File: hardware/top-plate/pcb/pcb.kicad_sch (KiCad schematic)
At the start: 43 parts, among them SW1 MT-0-102-A101-M200-RS+PJ

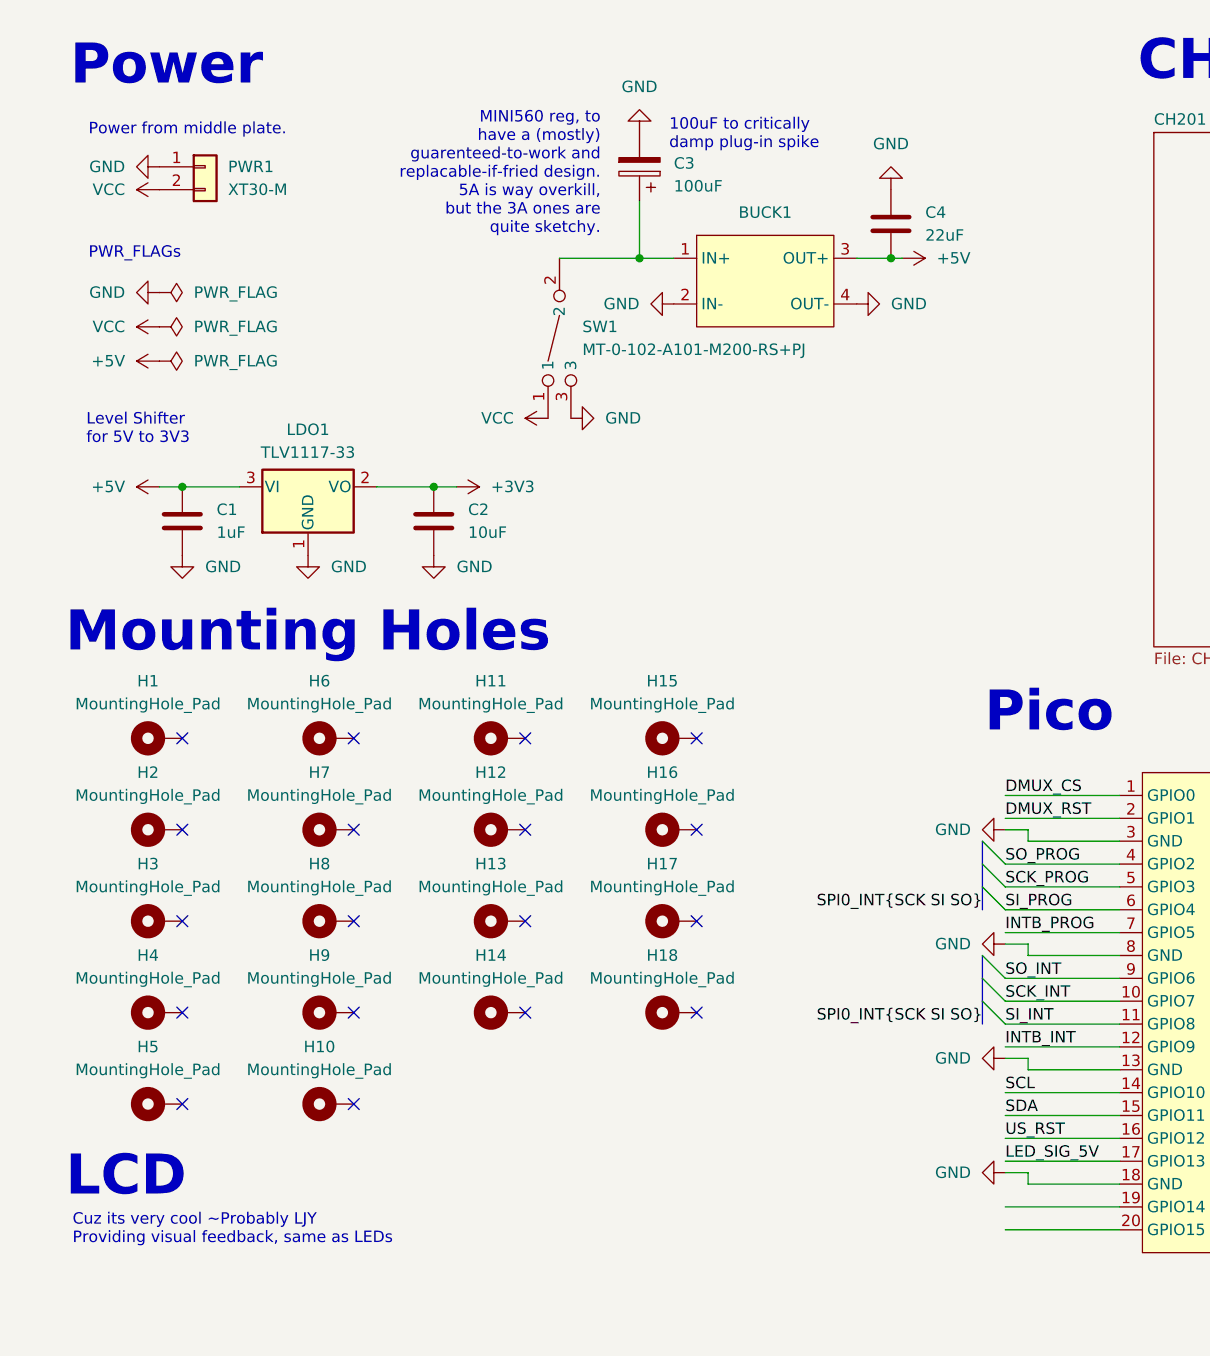
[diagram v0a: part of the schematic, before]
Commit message: changed some reference designators, and cleaned up schematics
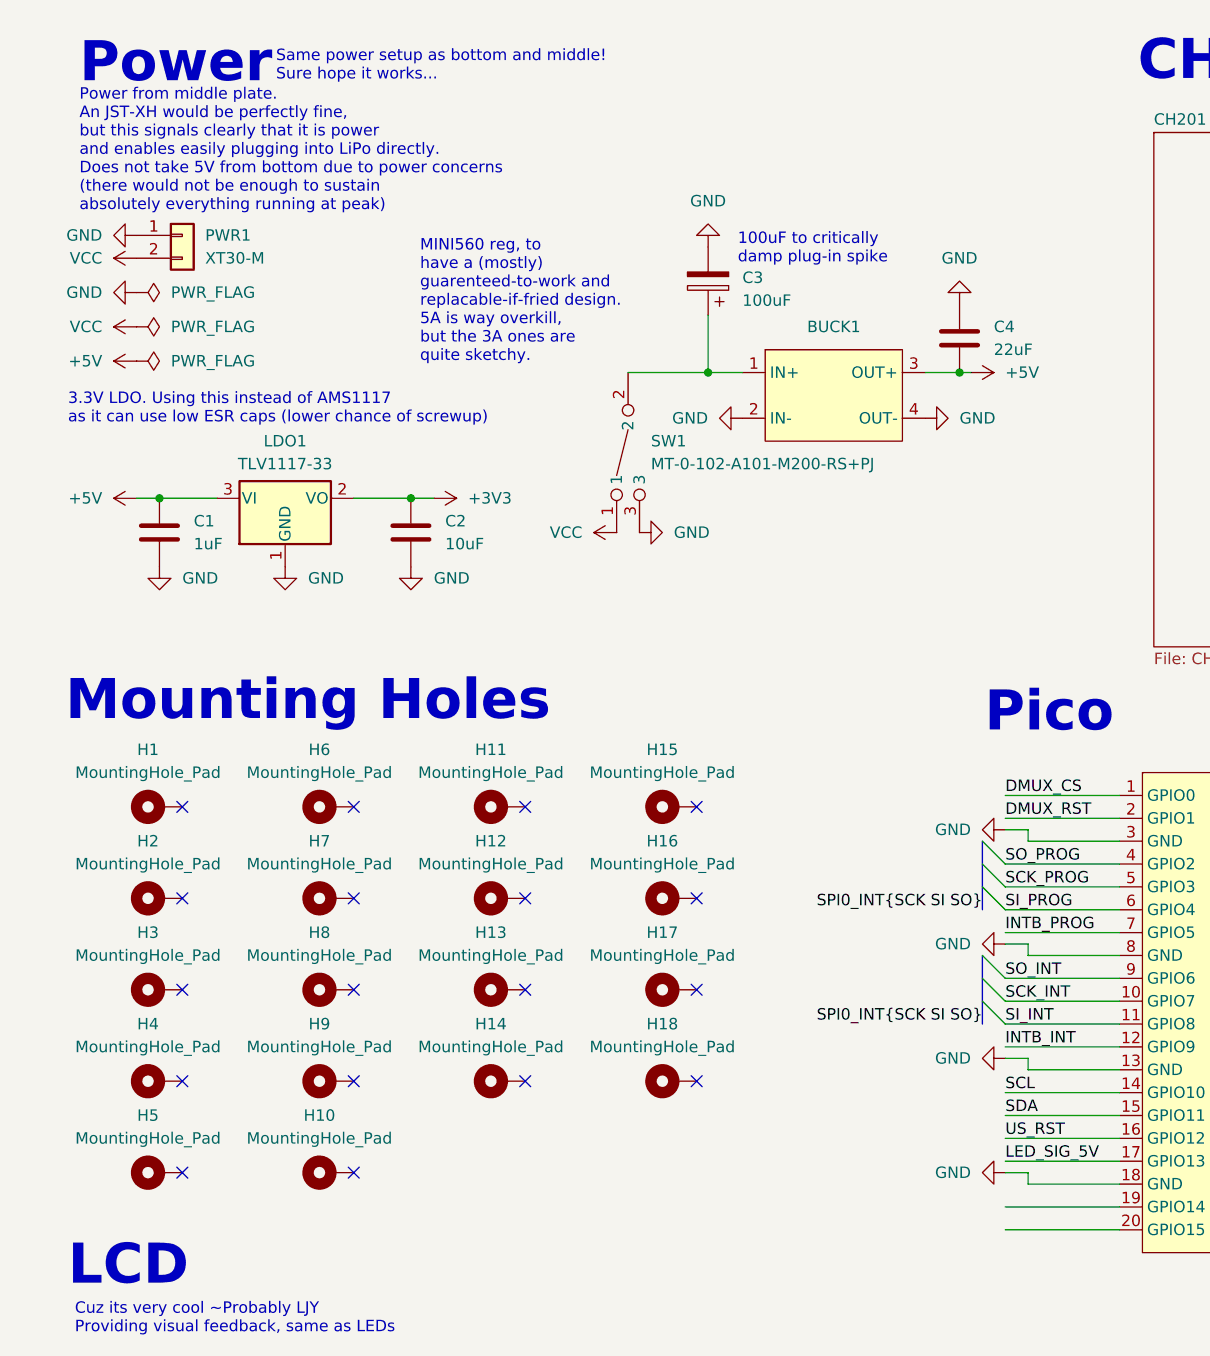
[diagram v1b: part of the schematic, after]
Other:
- note added: "3.3V LDO. Using this instead of AMS1117 as it can use low ESR caps (lower chance of screwup)"
- note added: "Power from middle plate. An JST-XH would be perfectly fine, but this signals clearly that it is power and enables easily plugging into LiPo directly. Does not take 5V from bottom due to power concerns (there would not be enough to sustain absolutely everything running at peak)"
- note added: "Same power setup as bottom and middle! Sure hope it works..."
- note removed: "Level Shifter for 5V to 3V3"
- note removed: "PWR_FLAGs"
- note removed: "Power from middle plate."
- moved on the sheet: BUCK1, C1, C2, C3, C4, H1, H10, H11, H12, H13, H14, H15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

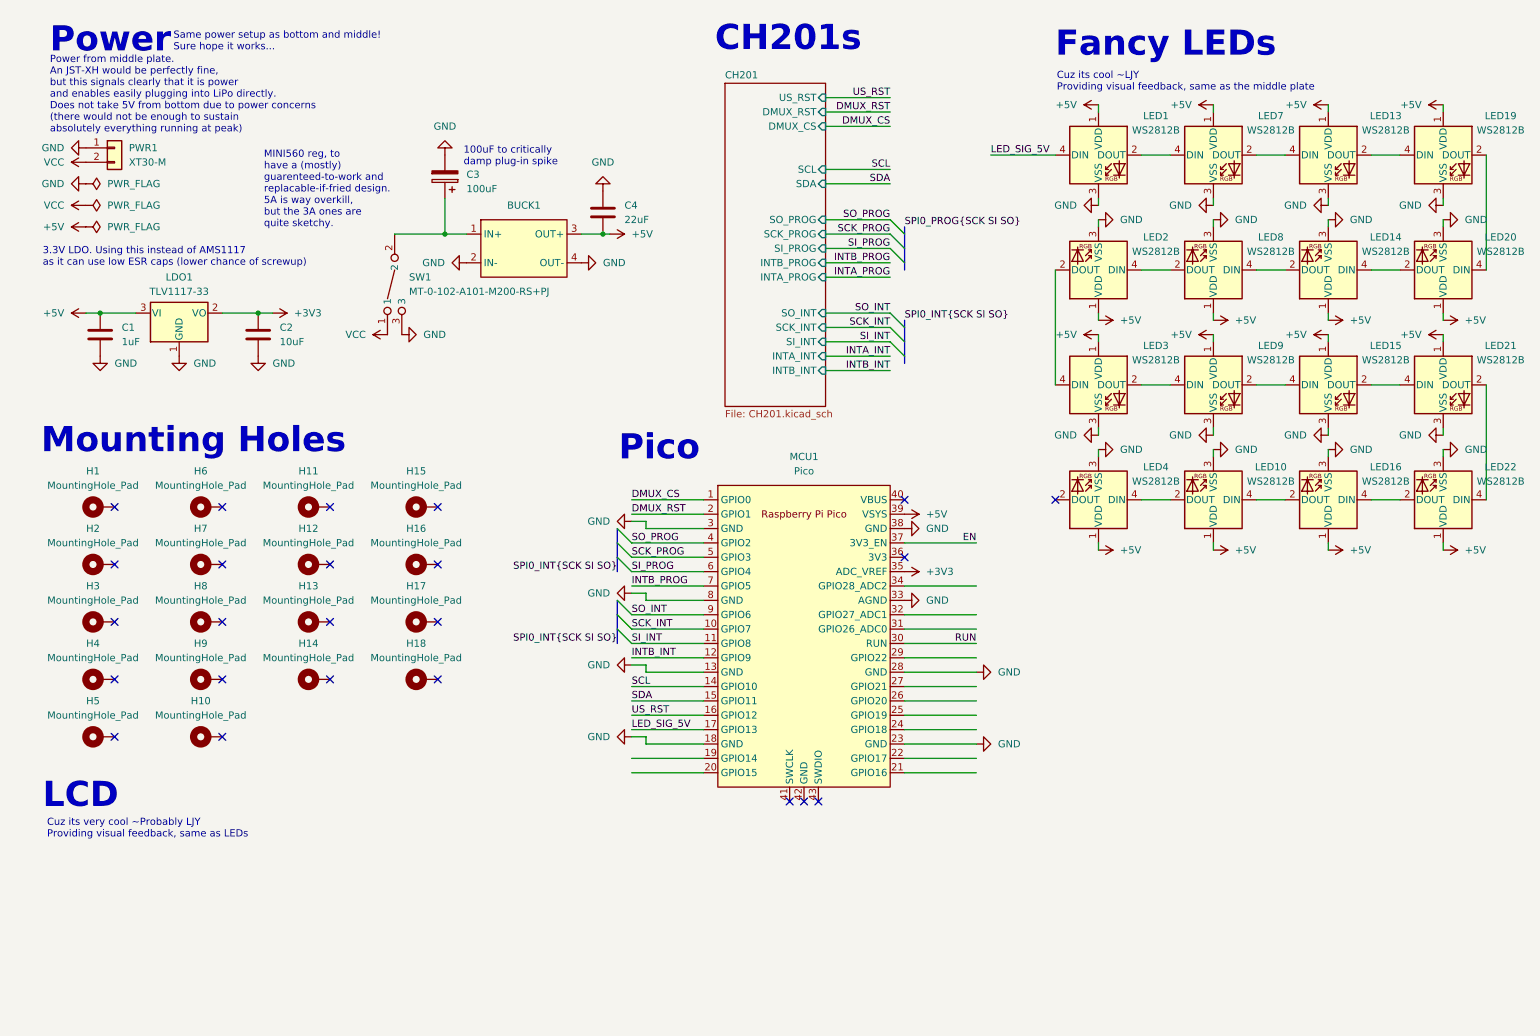
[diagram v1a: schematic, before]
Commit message: top plate schematic
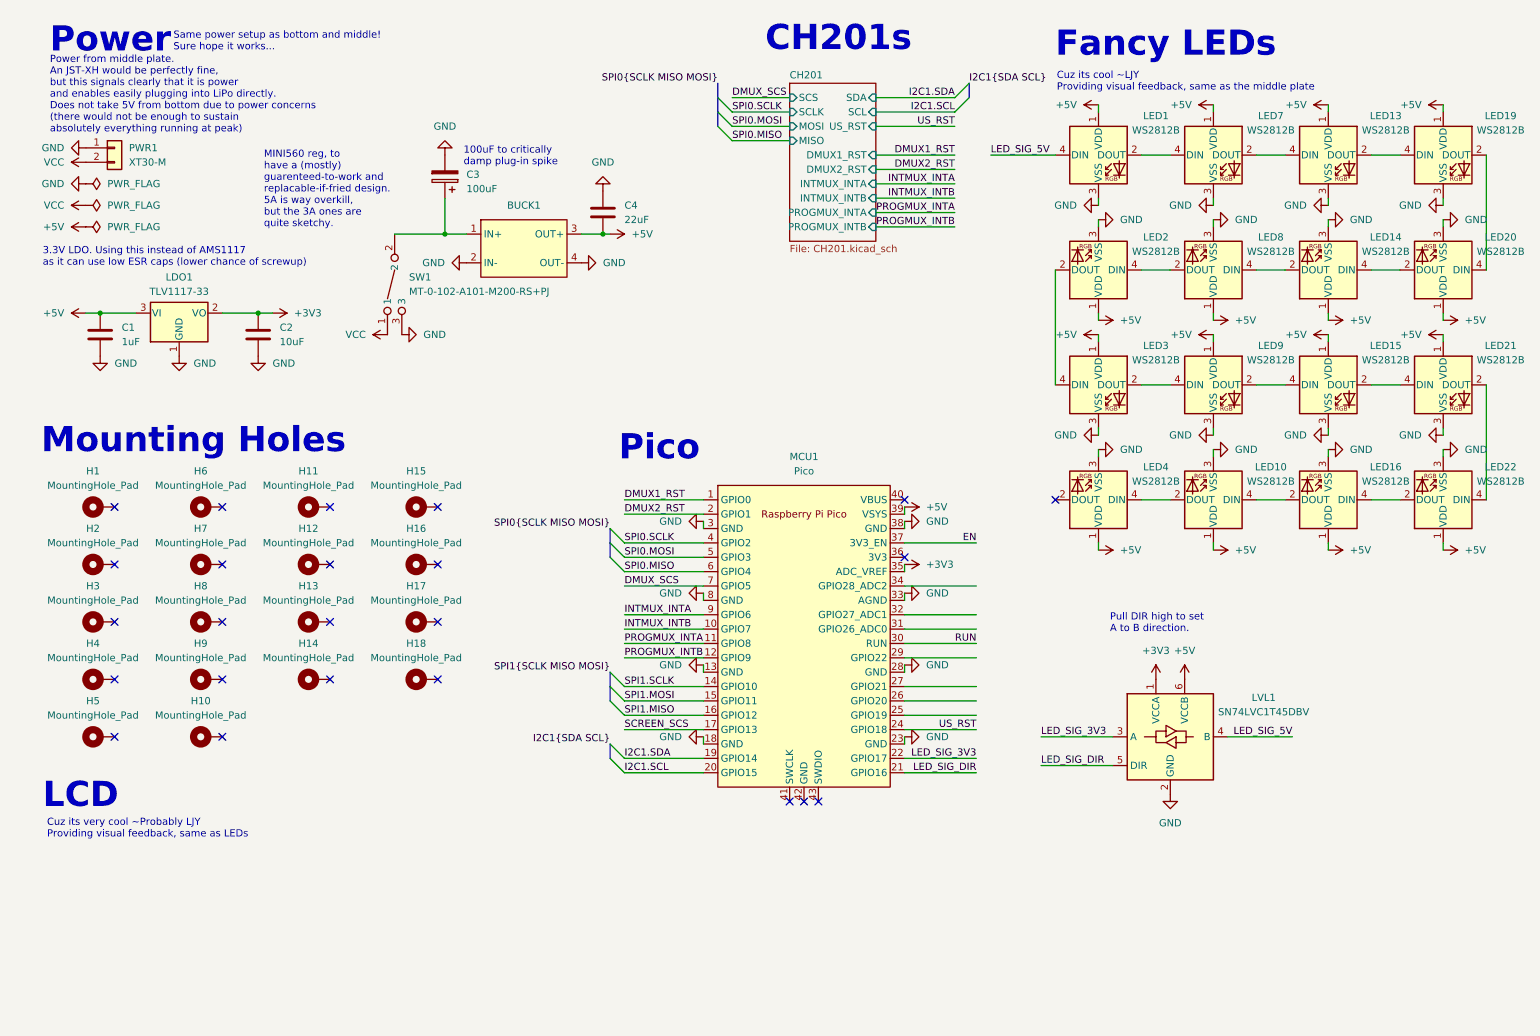
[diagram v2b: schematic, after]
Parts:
- added LVL1: SN74LVC1T45DBV, Package_TO_SOT_SMD:SOT-23-6, symbol Logic_LevelTranslator:SN74LVC1T45DBV
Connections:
- net +3V3: now also LVL1.1 (VCCA)
- net +5V: now also LVL1.6 (VCCB)
- net GND: now also LVL1.2 (GND)
- net LED_SIG_5V: now also LVL1.4 (B); no longer MCU1.17 (GPIO13)
- net US_RST: now also MCU1.24 (GPIO18); no longer MCU1.16 (GPIO12)
- net I2C1.SDA: now reaches MCU1.19 (GPIO14)
- net I2C1.SCL: now reaches MCU1.20 (GPIO15)
- net LED_SIG_DIR: now reaches MCU1.21 (GPIO16)
- net LED_SIG_DIR: now also LVL1.5 (DIR)
- net LED_SIG_3V3: now reaches MCU1.22 (GPIO17)
- net LED_SIG_3V3: now also LVL1.3 (A)
- net DMUX_CS renamed DMUX1_RST
- net DMUX_RST renamed DMUX2_RST
- net INTB_INT renamed PROGMUX_INTB
- net INTB_PROG renamed DMUX_SCS
- net SCK_INT renamed INTMUX_INTB
- net SCK_PROG renamed SPI0.MOSI
- net SCL renamed SPI1.SCLK
- net SDA renamed SPI1.MOSI
- net SI_INT renamed PROGMUX_INTA
- net SI_PROG renamed SPI0.MISO
- net SO_INT renamed INTMUX_INTA
- net SO_PROG renamed SPI0.SCLK
- new net SCREEN_SCS: MCU1.17 (GPIO13)
- new net SPI1.MISO: MCU1.16 (GPIO12)
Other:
- sheet CH201 ports: added DMUX1_RST, DMUX2_RST, INTMUX_INTA, INTMUX_INTB, MISO, MOSI, PROGMUX_INTA, PROGMUX_INTB, SCLK, SCS; removed DMUX_CS, DMUX_RST, INTA_INT, INTA_PROG, INTB_INT, INTB_PROG, SCK_INT, SCK_PROG, SI_INT, SI_PROG, SO_INT, SO_PROG
- note added: "Pull DIR high to set A to B direction."

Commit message: dunno
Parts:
- added C5: 1uF, PCM_Capacitor_SMD_AKL:C_1206_3216Metric_Pad1.33x1.80mm_HandSolder, symbol Device:C
- added C6: 10uF, PCM_Capacitor_SMD_AKL:C_1206_3216Metric_Pad1.33x1.80mm_HandSolder, symbol Device:C
- added LDO2: TLV1117-33, Package_TO_SOT_SMD:SOT-223-3_TabPin2, symbol Regulator_Linear:TLV1117-33
- added U1: RP2040-ZERO, Snapeda:RP2040-ZERO_MODULE_RP2040-ZERO, symbol Snapeda:RP2040-ZERO
- C2: renamed from C4; footprint PCM_Capacitor_SMD_AKL:C_0805_2012Metric_Pad1.15x1.40mm_HandSolder -> PCM_Capacitor_SMD_AKL:C_1206_3216Metric_Pad1.33x1.80mm_HandSolder
- C3: renamed from C1; footprint PCM_Capacitor_SMD_AKL:C_0805_2012Metric_Pad1.15x1.40mm_HandSolder -> PCM_Capacitor_SMD_AKL:C_1206_3216Metric_Pad1.33x1.80mm_HandSolder
- C4: renamed from C2; footprint PCM_Capacitor_SMD_AKL:C_0805_2012Metric_Pad1.15x1.40mm_HandSolder -> PCM_Capacitor_SMD_AKL:C_1206_3216Metric_Pad1.33x1.80mm_HandSolder
- LED1: footprint LED_SMD:LED_WS2812B-Mini_PLCC4_3.5x3.5mm -> LED_SMD:LED_WS2812B_PLCC4_5.0x5.0mm_P3.2mm
- LED10: renamed from LED9; footprint LED_SMD:LED_WS2812B-Mini_PLCC4_3.5x3.5mm -> LED_SMD:LED_WS2812B_PLCC4_5.0x5.0mm_P3.2mm
- LED11: renamed from LED15; footprint LED_SMD:LED_WS2812B-Mini_PLCC4_3.5x3.5mm -> LED_SMD:LED_WS2812B_PLCC4_5.0x5.0mm_P3.2mm
- LED12: renamed from LED21; footprint LED_SMD:LED_WS2812B-Mini_PLCC4_3.5x3.5mm -> LED_SMD:LED_WS2812B_PLCC4_5.0x5.0mm_P3.2mm
- LED13: renamed from LED4; footprint LED_SMD:LED_WS2812B-Mini_PLCC4_3.5x3.5mm -> LED_SMD:LED_WS2812B_PLCC4_5.0x5.0mm_P3.2mm
- LED14: renamed from LED10; footprint LED_SMD:LED_WS2812B-Mini_PLCC4_3.5x3.5mm -> LED_SMD:LED_WS2812B_PLCC4_5.0x5.0mm_P3.2mm
- LED15: renamed from LED16; footprint LED_SMD:LED_WS2812B-Mini_PLCC4_3.5x3.5mm -> LED_SMD:LED_WS2812B_PLCC4_5.0x5.0mm_P3.2mm
- LED16: renamed from LED22; footprint LED_SMD:LED_WS2812B-Mini_PLCC4_3.5x3.5mm -> LED_SMD:LED_WS2812B_PLCC4_5.0x5.0mm_P3.2mm
- LED2: renamed from LED7; footprint LED_SMD:LED_WS2812B-Mini_PLCC4_3.5x3.5mm -> LED_SMD:LED_WS2812B_PLCC4_5.0x5.0mm_P3.2mm
- LED3: renamed from LED13; footprint LED_SMD:LED_WS2812B-Mini_PLCC4_3.5x3.5mm -> LED_SMD:LED_WS2812B_PLCC4_5.0x5.0mm_P3.2mm
- LED4: renamed from LED19; footprint LED_SMD:LED_WS2812B-Mini_PLCC4_3.5x3.5mm -> LED_SMD:LED_WS2812B_PLCC4_5.0x5.0mm_P3.2mm
- LED5: renamed from LED2; footprint LED_SMD:LED_WS2812B-Mini_PLCC4_3.5x3.5mm -> LED_SMD:LED_WS2812B_PLCC4_5.0x5.0mm_P3.2mm
- LED6: renamed from LED8; footprint LED_SMD:LED_WS2812B-Mini_PLCC4_3.5x3.5mm -> LED_SMD:LED_WS2812B_PLCC4_5.0x5.0mm_P3.2mm
- LED7: renamed from LED14; footprint LED_SMD:LED_WS2812B-Mini_PLCC4_3.5x3.5mm -> LED_SMD:LED_WS2812B_PLCC4_5.0x5.0mm_P3.2mm
- LED8: renamed from LED20; footprint LED_SMD:LED_WS2812B-Mini_PLCC4_3.5x3.5mm -> LED_SMD:LED_WS2812B_PLCC4_5.0x5.0mm_P3.2mm
- LED9: renamed from LED3; footprint LED_SMD:LED_WS2812B-Mini_PLCC4_3.5x3.5mm -> LED_SMD:LED_WS2812B_PLCC4_5.0x5.0mm_P3.2mm
- renumbered C3 to C1
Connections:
- net +3V3: now also C5.2, LDO2.3 (VI)
- net +5V: now also U1.23 (5V)
- net DMUX1_RST: now also U1.1 (GP0)
- net DMUX2_RST: now also U1.2 (GP1)
- net DMUX_SCS: now also U1.6 (GP5)
- net GND: now also C5.1, C6.1, LDO2.1 (GND), U1.22 (GND)
- net I2C1.SCL: now also U1.15 (GP14)
- net I2C1.SDA: now also U1.16 (GP15)
- net INTMUX_INTA: now also U1.7 (GP6)
- net INTMUX_INTB: now also U1.8 (GP7)
- net LED_SIG_3V3: now also U1.17 (GP26)
- net LED_SIG_DIR: now also U1.18 (GP27)
- net PROGMUX_INTA: now also U1.9 (GP8)
- net PROGMUX_INTB: now also U1.10 (GP9)
- net SCREEN_SCS: now also U1.14 (GP13)
- net SPI0.MISO: now also U1.5 (GP4)
- net SPI0.MOSI: now also U1.4 (GP3)
- net SPI0.SCLK: now also U1.3 (GP2)
- net SPI1.MISO: now also U1.13 (GP12)
- net SPI1.MOSI: now also U1.12 (GP11)
- net SPI1.SCLK: now also U1.11 (GP10)
- net US_RST: now also U1.19 (GP28)
- new net +1V8: C6.2, LDO2.2 (VO)
- no-connect marks 24 -> 25
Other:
- moved on the sheet: BUCK1, C1, C2, SW1
